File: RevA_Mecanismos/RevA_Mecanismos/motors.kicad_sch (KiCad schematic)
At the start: 36 parts, among them J10 Conn_01x08_Socket, J11 Conn_01x03_Pin, J12 430450624, J13 Screw_Terminal_01x02, J14 Screw_Terminal_01x02, J15 Conn_01x03_Pin, J16 430450624, J9 Conn_01x08_Socket, Q3 IRF9540NSPBF, Q4 IRF9540NSPBF, Q5 IRF9540NSPBF, Q6 IRF9540NSPBF, U4 IRF540SPBF, U5 IRF540SPBF, U6 IRF540SPBF, U7 IRF540SPBF, U8 TXB0104D

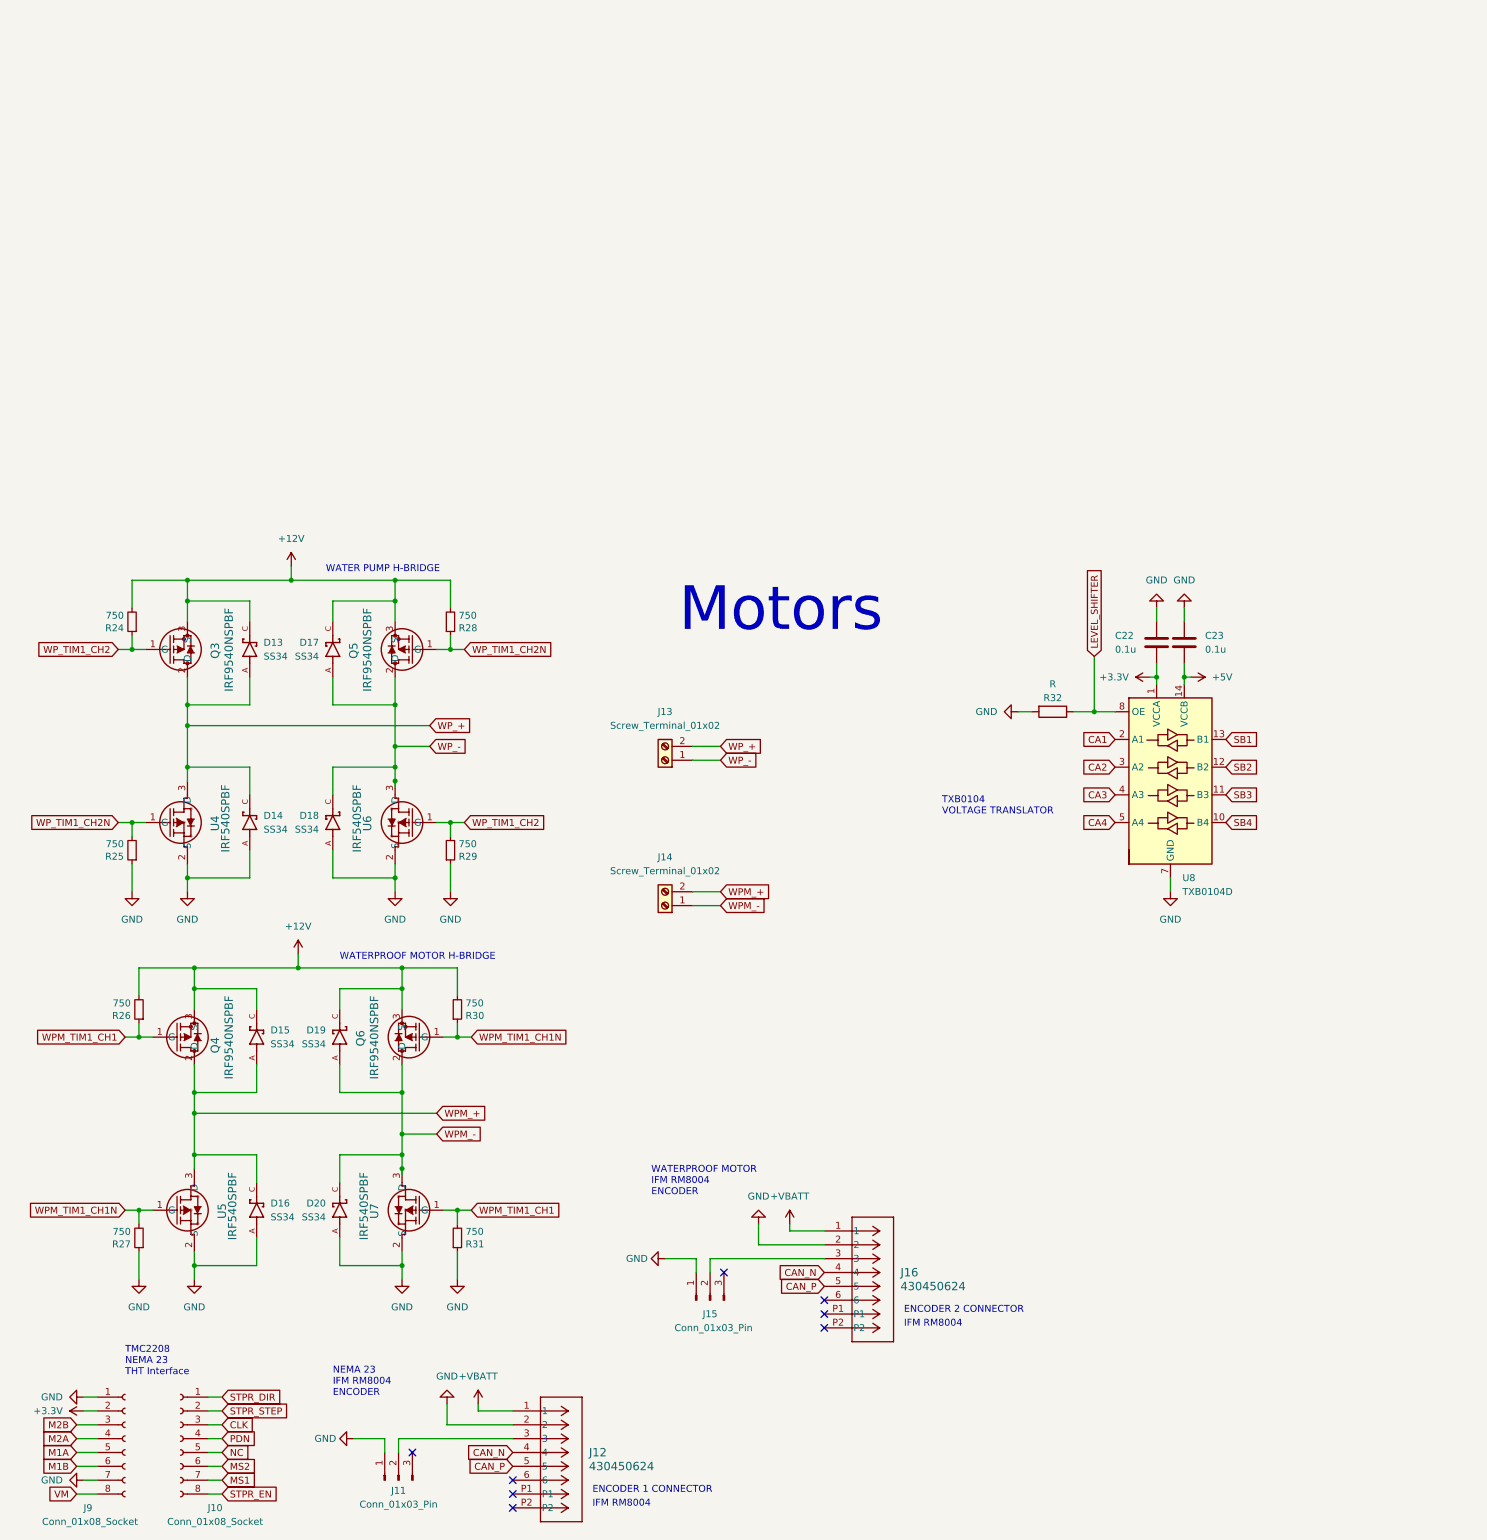
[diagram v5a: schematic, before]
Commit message: Complete schematic and pcb designs, routes missing and not yet complete
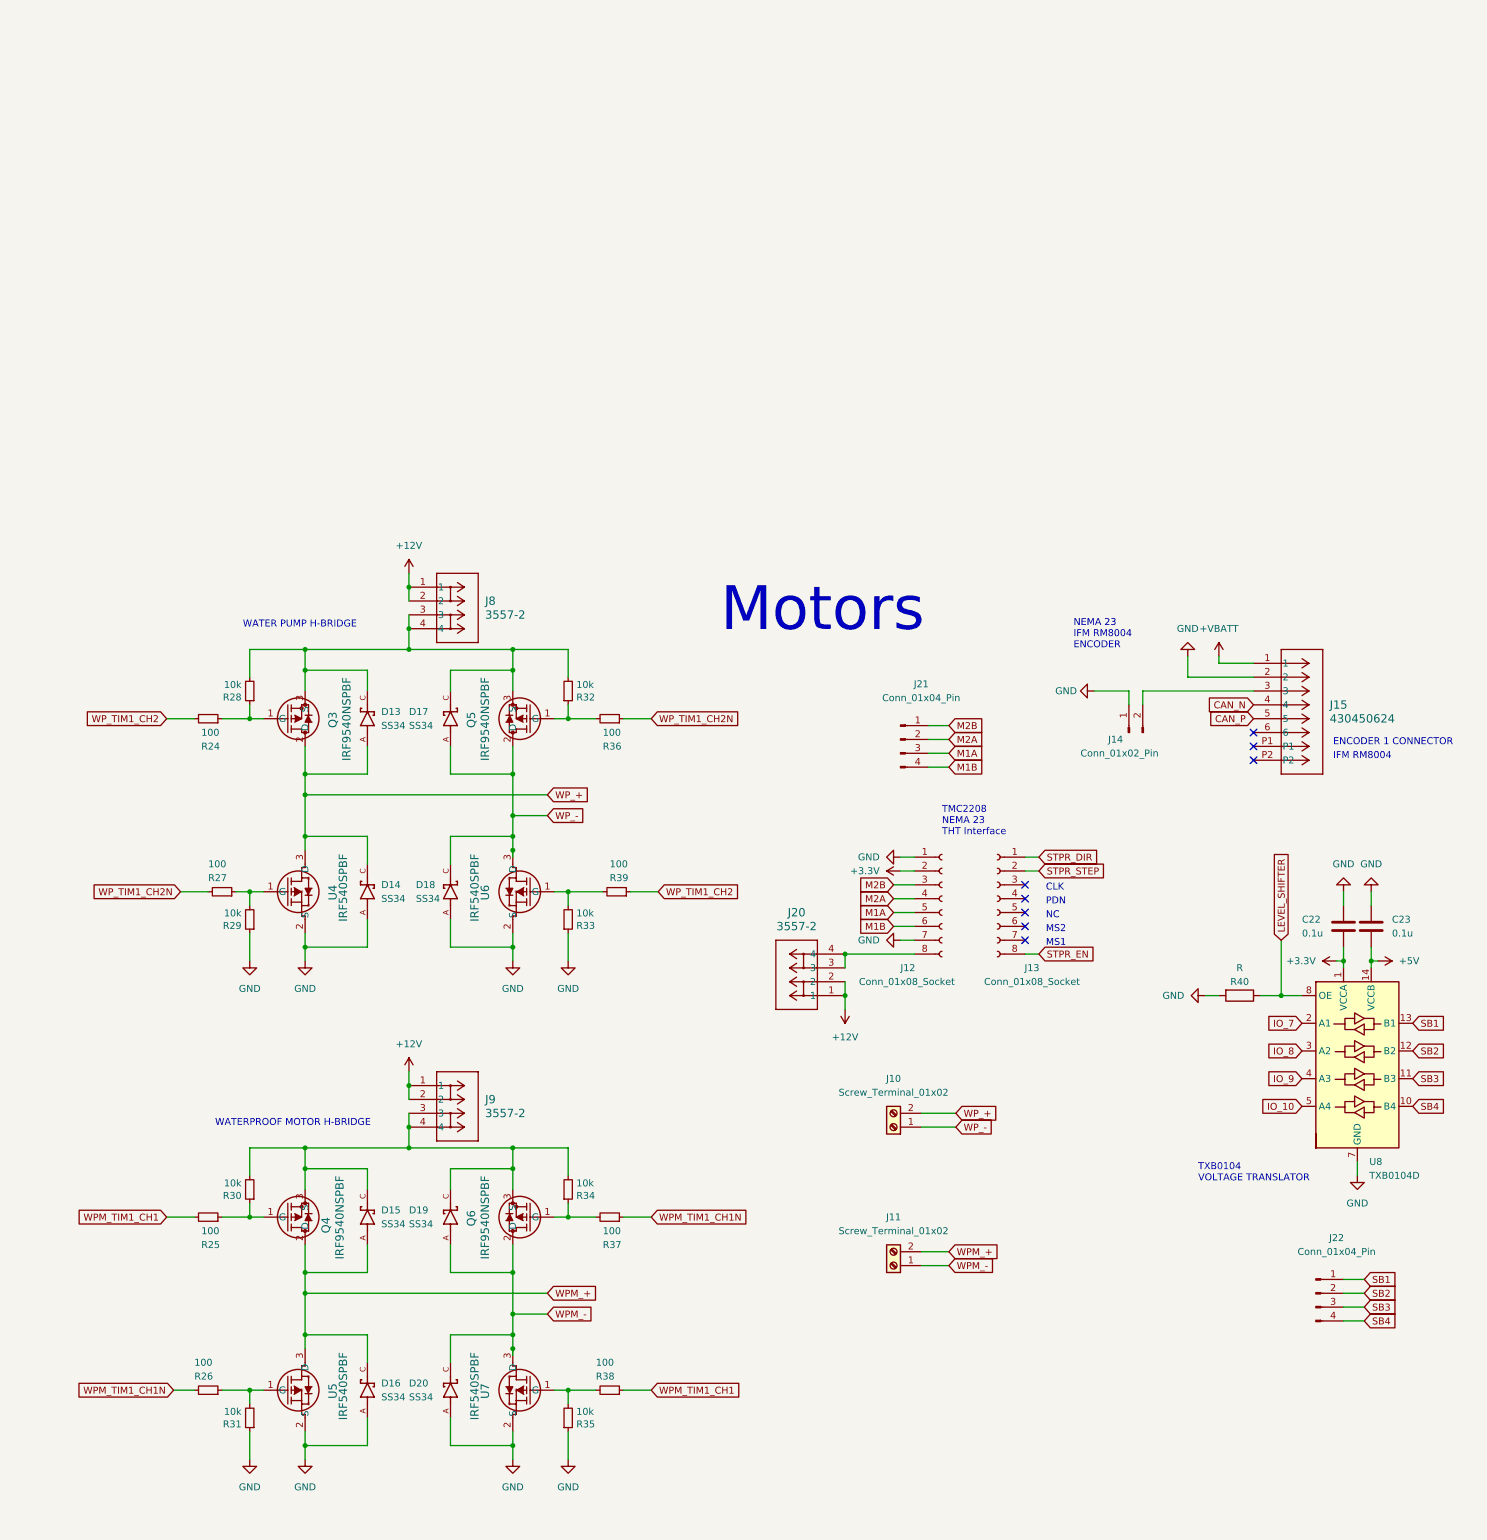
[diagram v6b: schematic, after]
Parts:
- removed J11, J15: Conn_01x03_Pin, Connector_PinHeader_2.54mm:PinHeader_1x03_P2.54mm_Vertical, symbol Connector:Conn_01x03_Pin
- removed J13, J14: Screw_Terminal_01x02, TerminalBlock:TerminalBlock_Altech_AK300-2_P5.00mm, symbol Connector:Screw_Terminal_01x02
- removed J16: 430450624, MolexConnectors:CON_430450624_MOL, symbol MolexConnectors:430450624
- added J10, J11: Screw_Terminal_01x02, symbol Connector:Screw_Terminal_01x02
- added J14: Conn_01x02_Pin, Connector_PinHeader_2.54mm:PinHeader_1x07_P2.54mm_Vertical, symbol Connector:Conn_01x02_Pin
- added J20: 3557-2, TerminalBlock:TerminalBlock_Altech_AK300-2_P5.00mm, symbol 36-3557-2-ND:3557-2
- added J21: Conn_01x04_Pin, TerminalBlock:TerminalBlock_Altech_AK300-2_P5.00mm, symbol Connector:Conn_01x04_Pin
- added J22: Conn_01x04_Pin, Connector_PinHeader_2.54mm:PinHeader_1x02_P2.54mm_Vertical, symbol Connector:Conn_01x04_Pin
- added J8, J9: 3557-2, 36-3557-2-ND:CONN_3557-2_KEY, symbol 36-3557-2-ND:3557-2
- added R24, R25, R26, R27, R36, R37, R38, R39: 100, Resistor_SMD:R_0603_1608Metric, symbol Device:R_Small
- D13, D14, D15, D16, D17, D18, D19, D20: footprint SS34:SS34 -> SS34:DIOM7959X265N
- J13: renamed from J10; footprint Connector_PinSocket_2.54mm:PinSocket_1x08_P2.54mm_Vertical -> MolexConnectors:CON_430450624_MOL
- J15: renamed from J12; footprint MolexConnectors:CON_430450624_MOL -> Connector_PinHeader_2.54mm:PinHeader_1x02_P2.54mm_Vertical
- Q3, Q4, Q5, Q6: footprint PMOSGDS_D2PAK_INF -> IRF9540NSPBF:PMOSGDS_D2PAK_INF
- R28: renamed from R24; value 750 -> 10k
- R29: renamed from R25; value 750 -> 10k
- R30: renamed from R26; value 750 -> 10k
- R31: renamed from R27; value 750 -> 10k
- R32: renamed from R28; value 750 -> 10k
- R33: renamed from R29; value 750 -> 10k
- R34: renamed from R30; value 750 -> 10k
- R35: renamed from R31; value 750 -> 10k
- U4, U5, U6, U7: footprint D2PAK_VIS -> IRF540SPBF:D2PAK_VIS
- renumbered J9 to J12, R32 to R40
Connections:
- net +12V: now also J20.1, J20.2, J8.1, J8.2, J9.1, J9.2; no longer D13.C, D15.C, D17.C, D19.C, Q3.3 (S), Q4.3 (S), Q5.3 (S), Q6.3 (S), R28.2, R30.2, R32.2, R34.2
- net GND: now also J14.1 (Pin_1)
- net M1A: now also J21.3 (Pin_3)
- net M1B: now also J21.4 (Pin_4)
- net M2A: now also J21.2 (Pin_2)
- net M2B: now also J21.1 (Pin_1)
- net SB1: now also J22.1 (Pin_1)
- net SB2: now also J22.2 (Pin_2)
- net SB3: now also J22.3 (Pin_3)
- net SB4: now also J22.4 (Pin_4)
- net WPM_+: now also J11.2 (Pin_2)
- net WPM_-: now also J11.1 (Pin_1)
- net WPM_TIM1_CH1: now also R25.2, R38.1; no longer Q4.1 (G), R30.1, R35.2, U7.1 (G)
- net WPM_TIM1_CH1N: now also R26.2, R37.1; no longer Q6.1 (G), R31.2, R34.1, U5.1 (G)
- net WP_+: now also J10.2 (Pin_2)
- net WP_-: now also J10.1 (Pin_1)
- net WP_TIM1_CH2: now also R24.2, R39.1; no longer Q3.1 (G), R28.1, R33.2, U6.1 (G)
- net WP_TIM1_CH2N: now also R27.2, R36.1; no longer Q5.1 (G), R29.2, R32.1, U4.1 (G)
- net at J15.3: now also J14.2 (Pin_2)
- net CA1 renamed IO_7
- net CA2 renamed IO_8
- net CA3 renamed IO_9
- net CA4 renamed IO_10
- net CLK: no longer names the net of J13.3 (Pin_3)
- net MS1: no longer names the net of J13.7 (Pin_7)
- net MS2: no longer names the net of J13.6 (Pin_6)
- net NC: no longer names the net of J13.5 (Pin_5)
- net PDN: no longer names the net of J13.4 (Pin_4)
- net VM: no longer names the net of J12.8 (Pin_8)
- net VM: now also J20.3, J20.4
- new net: R27.1, R29.2, U4.1 (G)
- new net: R33.2, R39.2, U6.1 (G)
- new net: R35.2, R38.2, U7.1 (G)
- new net: Q6.1 (G), R34.1, R37.2
- new net: D15.C, D19.C, J9.3, J9.4, Q4.3 (S), Q6.3 (S), R30.2, R34.2
- new net: D13.C, D17.C, J8.3, J8.4, Q3.3 (S), Q5.3 (S), R28.2, R32.2
- new net: R26.1, R31.2, U5.1 (G)
- new net: Q5.1 (G), R32.1, R36.2
- new net: Q3.1 (G), R24.1, R28.1
- new net: Q4.1 (G), R25.1, R30.1
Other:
- note added: "CLK"
- note added: "MS1"
- note added: "MS2"
- note added: "NC"
- note added: "PDN"
- note removed: "ENCODER 2 CONNECTOR"
- note removed: "WATERPROOF MOTOR IFM RM8004 ENCODER"
- moved on the sheet: C22, C23, D13, D14, D15, D16, D17, D18, D19, D20, J12, J13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

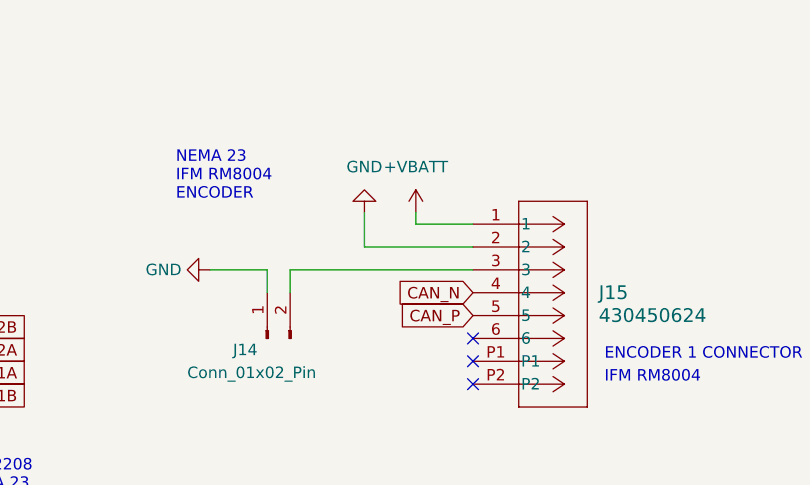
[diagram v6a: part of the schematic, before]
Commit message: Correction made to footprint for J3 pin header
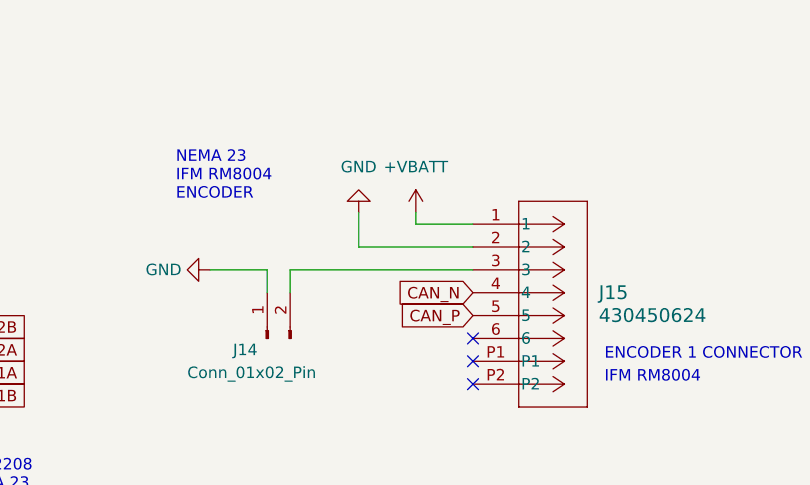
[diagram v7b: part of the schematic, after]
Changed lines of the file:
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@@
-    (stroke (width 0) (type default))
-  )
-  (wire (pts (xy 226.695 36.83) (xy 226.695 40.64))
     (stroke (width 0) (type default))
   )
@@
     (stroke (width 0) (type default))
   )
+  (wire (pts (xy 226.06 36.83) (xy 226.06 40.64))
+    (stroke (width 0) (type default))
+  )
   (wire (pts (xy 172.72 81.28) (xy 176.53 81.28))
     (stroke (width 0) (type default))
@@
     (stroke (width 0) (type default))
   )
-  (wire (pts (xy 238.76 40.64) (xy 226.695 40.64))
-    (stroke (width 0) (type default))
-  )
   (wire (pts (xy 255.27 92.71) (xy 255.27 93.98))
     (stroke (width 0) (type default))
@@
   )
   (wire (pts (xy 54.61 35.56) (xy 64.77 35.56))
+    (stroke (width 0) (type default))
+  )
+  (wire (pts (xy 226.06 40.64) (xy 238.76 40.64))
     (stroke (width 0) (type default))
   )
@@
     )
   )
-  (symbol (lib_id "power:GND") (at 226.695 36.83 180) (unit 1)
-    (in_bom yes) (on_board yes) (dnp no) (fields_autoplaced)
-    (property "Reference" "#PWR082" (at 226.695 30.48 0)
-      (effects (font (size 1.27 1.27)) hide)
-    )
-    (property "Value" "GND" (at 226.695 31.75 0)
+  (symbol (lib_id "power:GND") (at 226.06 36.83 0) (mirror x) (unit 1)
+    (in_bom yes) (on_board yes) (dnp no)
+    (property "Reference" "#PWR082" (at 226.06 30.48 0)
+      (effects (font (size 1.27 1.27)) hide)
+    )
+    (property "Value" "GND" (at 226.06 31.75 0)
       (effects (font (size 1.27 1.27)))
     )
-    (property "Footprint" "" (at 226.695 36.83 0)
-      (effects (font (size 1.27 1.27)) hide)
-    )
-    (property "Datasheet" "" (at 226.695 36.83 0)
-      (effects (font (size 1.27 1.27)) hide)
-    )
+    (property "Footprint" "" (at 226.06 36.83 0)
+      (effects (font (size 1.27 1.27)) hide)
+    )
+    (property "Datasheet" "" (at 226.06 36.83 0)
+      (effects (font (size 1.27 1.27)) hide)
+    )

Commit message: PCB Routing completed
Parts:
- D19: footprint SS34:DIOM7959X265N -> SS34:SS34
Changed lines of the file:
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@@
       (effects (font (size 1.27 1.27)) (justify left))
     )
-    (property "Footprint" "SS34:DIOM7959X265N" (at 91.44 139.7 0)
+    (property "Footprint" "SS34:SS34" (at 91.44 139.7 0)
       (effects (font (size 1.27 1.27)) (justify bottom) hide)
     )
